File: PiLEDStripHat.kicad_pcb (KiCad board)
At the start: 2 copper layers, 65 x 30 mm, 13 parts, among them CON1 BARREL_JACK, J1 RPi_GPIO, P1 CONN_01X04, P2 CONN_01X02, U1 74AHC125

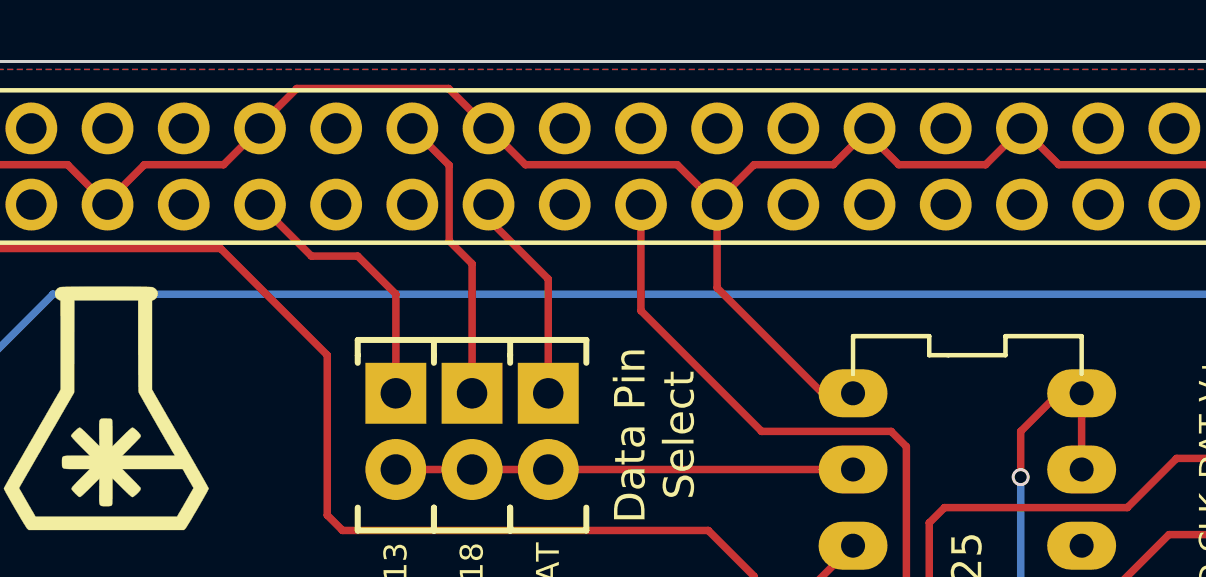
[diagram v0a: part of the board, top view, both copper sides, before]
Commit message: fixed GPIO mappings
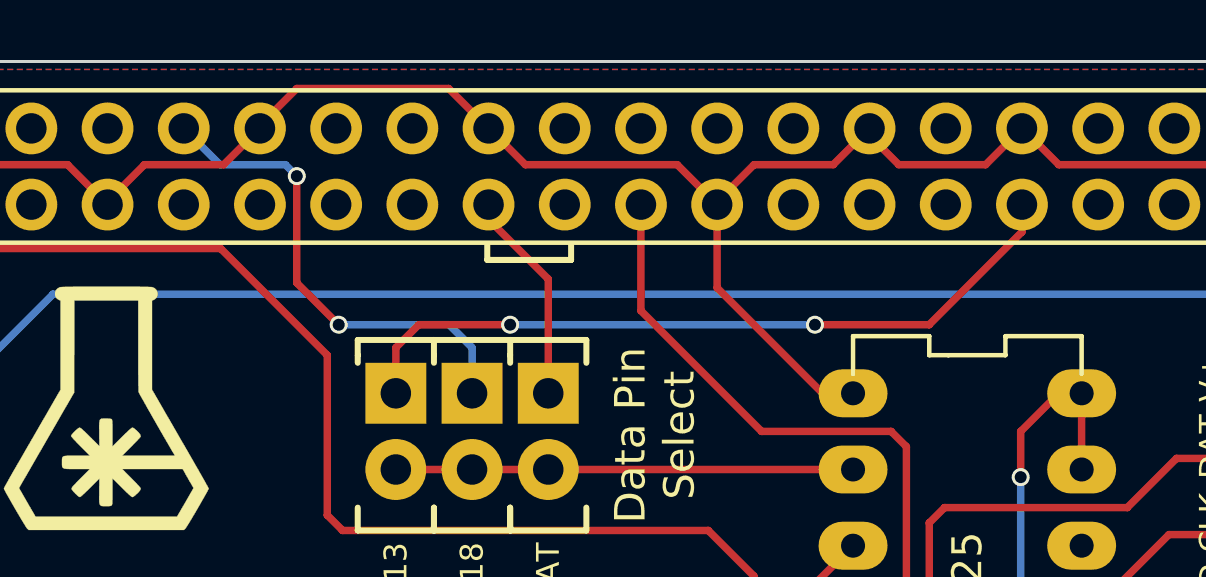
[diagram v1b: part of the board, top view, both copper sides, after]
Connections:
- J1 pad 12: Net-(J1-Pad12) -> PWM_18
- J1 pad 13: PWM_13 -> Net-(J1-Pad13)
- J1 pad 18: PWM_18 -> Net-(J1-Pad18)
- J1 pad 33: Net-(J1-Pad33) -> PWM_13
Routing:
- net PWM_13: track 9.07 -> 24.9 mm, vias 0 -> 2
- net PWM_18: track 9.65 -> 16.2 mm, vias 0 -> 2
